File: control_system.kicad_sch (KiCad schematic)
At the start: 0 parts

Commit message: add H-bridge schematic
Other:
- added sheet H-Bridge (HighVoltageHBridge.kicad_sch)
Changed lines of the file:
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@@
 	(generator_version "9.0")
 	(paper "A4")
+	(sheet
+		(at 177.8 97.79)
+		(size 46.99 25.4)
+		(exclude_from_sim no)
+		(in_bom yes)
+		(on_board yes)
+		(dnp no)
+		(fields_autoplaced yes)
+		(stroke
+			(width 0.1524)
+			(type solid)
+		)
+		(fill
+			(color 0 0 0 0.0000)
+		)
+		(property "Sheetname" "H-Bridge"
+			(at 177.8 97.0784 0)
+			(effects
+				(font
+					(size 1.27 1.27)
+				)
+				(justify left bottom)
+			)
+		)
+		(property "Sheetfile" "HighVoltageHBridge.kicad_sch"
+			(at 177.8 123.7746 0)
+			(effects
+				(font
+					(size 1.27 1.27)
+				)
+				(justify left top)
+			)
+		)
+		(instances
+			(project "Strain Wave Motor Control Board"
+				(path "/6a10ea30-147f-4e88-a5c3-bf0fd41178aa/9ffa4e09-e84e-481d-9a76-0a18653cd84d"
+					(page "4")
+				)
+			)
+		)
+	)
 )

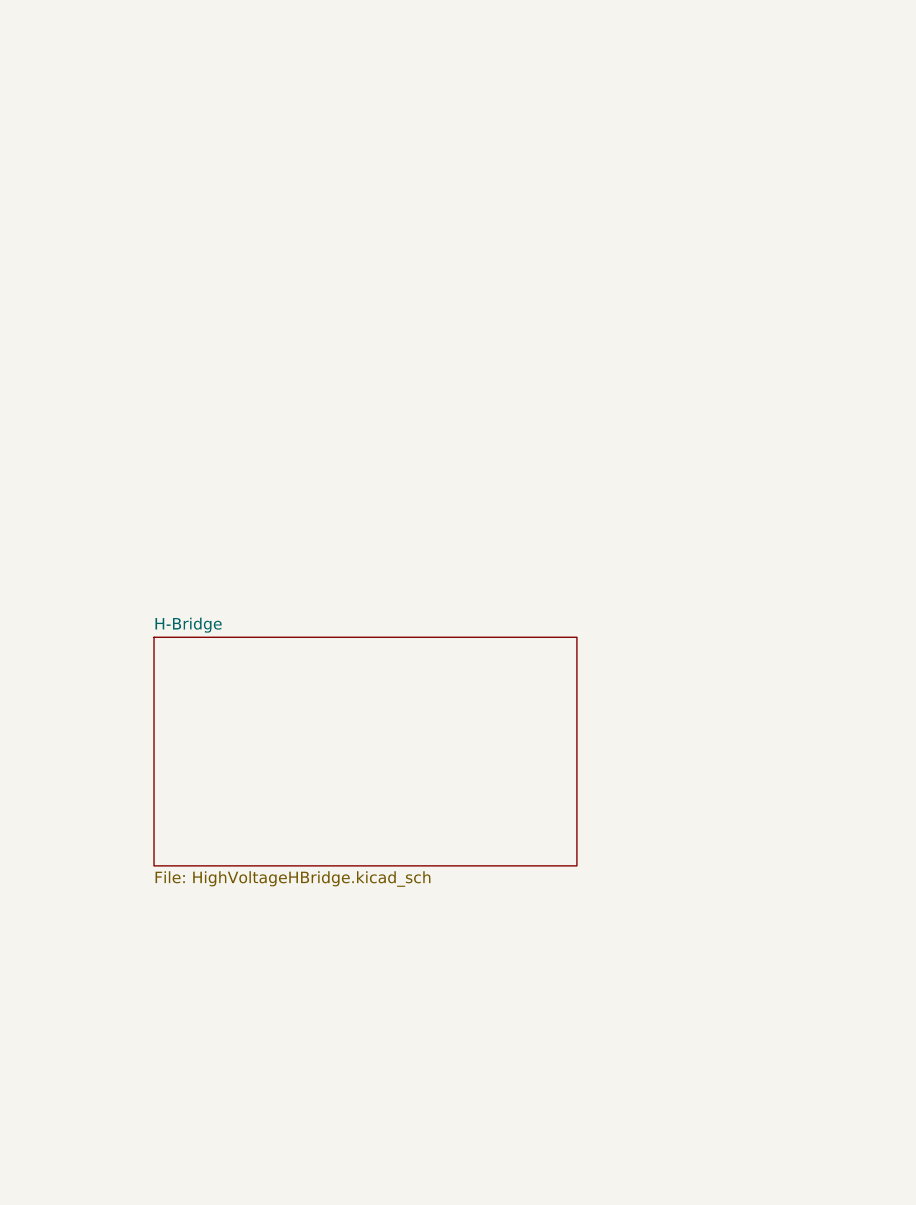
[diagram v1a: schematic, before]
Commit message: footprint issues solved
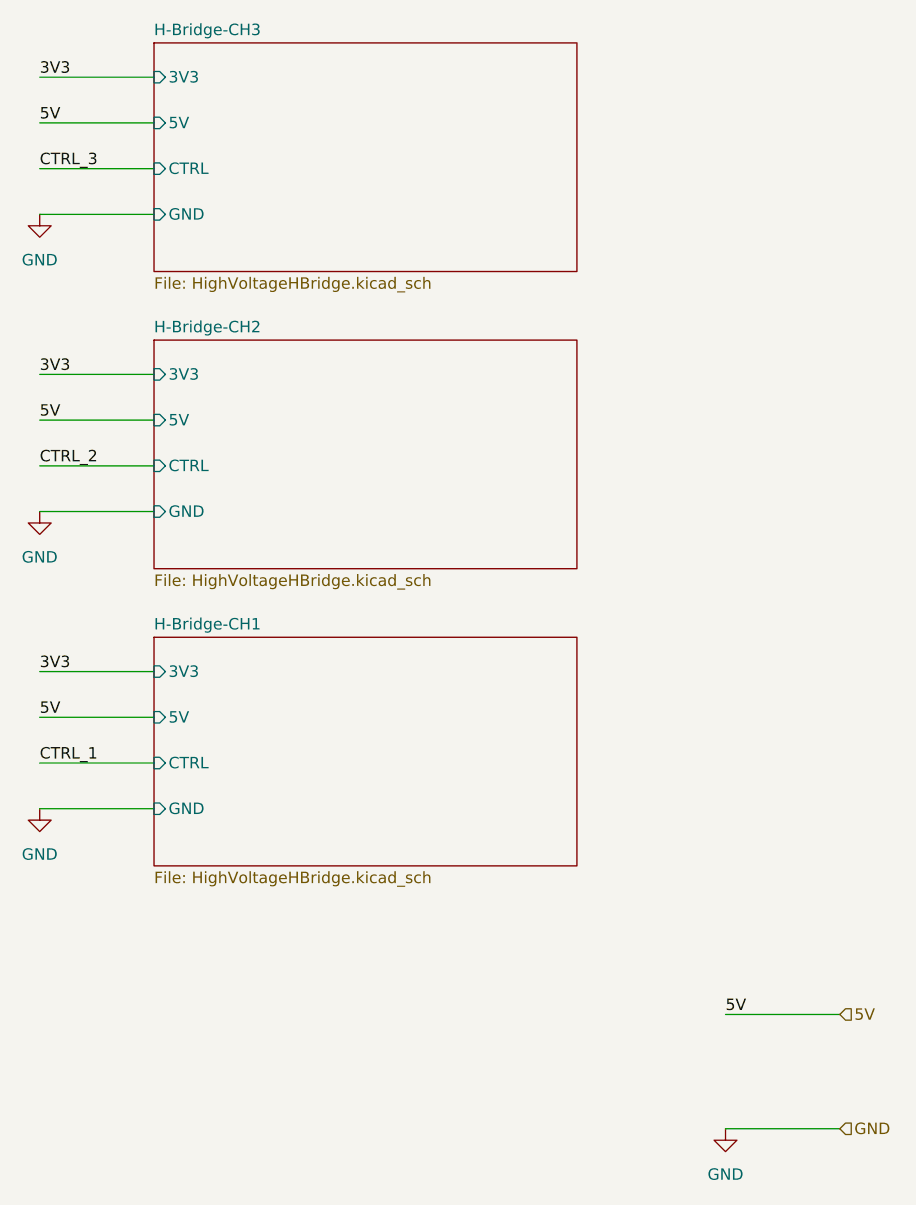
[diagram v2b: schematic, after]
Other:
- sheet H-Bridge renamed H-Bridge-CH1
- added sheet H-Bridge-CH2 (HighVoltageHBridge.kicad_sch)
- added sheet H-Bridge-CH3 (HighVoltageHBridge.kicad_sch)
- sheet H-Bridge-CH1 ports: added 3V3, 5V, CTRL, GND; removed none

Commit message: ESP32 schematic added
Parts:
- added J6, J7: Conn_01x16_Pin, symbol Connector:Conn_01x16_Pin
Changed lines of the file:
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@@
+	)
+	(symbol
+		(lib_id "Connector:Conn_01x16_Pin")
+		(at 43.18 49.53 0)
+		(unit 1)
+		(exclude_from_sim no)
+		(in_bom yes)
+		(on_board yes)
+		(dnp no)
+		(fields_autoplaced yes)
+		(property "Reference" "J6"
+			(at 43.815 26.67 0)
+			(effects
+				(font
+					(size 1.27 1.27)
+				)
+			)
+		)
+		(property "Value" "Conn_01x16_Pin"
+			(at 43.815 29.21 0)
+			(effects
+				(font
+					(size 1.27 1.27)
+				)
+			)
+		)
+		(property "Footprint" ""
+			(at 43.18 49.53 0)
+			(effects
+				(font
+					(size 1.27 1.27)
+				)
+				(hide yes)
+			)
+		)
+		(property "Datasheet" "~"
+			(at 43.18 49.53 0)
+			(effects
+				(font
+					(size 1.27 1.27)
+				)
+				(hide yes)
+			)
+		)
+		(property "Description" "Generic connector, single row, 01x16, script generated"
+			(at 43.18 49.53 0)
+			(effects
+				(font
+					(size 1.27 1.27)
+				)
+				(hide yes)
+			)
+		)
+		(pin "11"
+		)
+		(pin "10"
+		)
+		(pin "13"
+		)
+		(pin "15"
+		)
+		(pin "14"
+		)
+		(pin "16"
+		)
+		(pin "6"
+		)
+		(pin "7"
+		)
+		(pin "9"
+		)
+		(pin "12"
+		)
+		(pin "1"
+		)
+		(pin "8"
+		)
+		(pin "3"
+		)
+		(pin "4"
+		)
+		(pin "5"
+		)
+		(pin "2"
+		)
+		(instances
+			(project ""
+				(path "/6a10ea30-147f-4e88-a5c3-bf0fd41178aa/9ffa4e09-e84e-481d-9a76-0a18653cd84d"
+					(reference "J6")
+					(unit 1)
+				)
+			)
+		)
 	)
 	(symbol
@@
 					(unit 1)
 				)
+			)
+		)
+	)
+	(symbol
+		(lib_id "Connector:Conn_01x16_Pin")
+		(at 73.66 49.53 0)
+		(unit 1)
+		(exclude_from_sim no)
+		(in_bom yes)
+		(on_board yes)
+		(dnp no)
+		(fields_autoplaced yes)
+		(property "Reference" "J7"
+			(at 74.295 26.67 0)
+			(effects
+				(font
+					(size 1.27 1.27)
+				)
+			)
+		)
+		(property "Value" "Conn_01x16_Pin"
+			(at 74.295 29.21 0)
+			(effects
+				(font
+					(size 1.27 1.27)
+				)
+			)
+		)
+		(property "Footprint" ""
+			(at 73.66 49.53 0)
+			(effects
+				(font
+					(size 1.27 1.27)
+				)
+				(hide yes)
+			)
+		)
+		(property "Datasheet" "~"
+			(at 73.66 49.53 0)
+			(effects
+				(font
+					(size 1.27 1.27)
+				)
+				(hide yes)
+			)
+		)
+		(property "Description" "Generic connector, single row, 01x16, script generated"
+			(at 73.66 49.53 0)
+			(effects
+				(font
+					(size 1.27 1.27)
+				)
+				(hide yes)
+			)
+		)
+		(pin "11"
+		)
+		(pin "10"
+		)
+		(pin "13"
+		)
+		(pin "15"
+		)
+		(pin "14"
+		)
+		(pin "16"
+		)
+		(pin "6"
+		)
+		(pin "7"
+		)
+		(pin "9"
+		)
+		(pin "12"
+		)
+		(pin "1"
+		)
+		(pin "8"
+		)
+		(pin "3"
+		)
+		(pin "4"
+		)
+		(pin "5"
+		)
+		(pin "2"
+		)
+		(instances
+			(project "Strain Wave Motor Control Board"
+				(path "/6a10ea30-147f-4e88-a5c3-bf0fd41178aa/9ffa4e09-e84e-481d-9a76-0a18653cd84d"
+					(reference "J7")
+					(unit 1)
+				)
